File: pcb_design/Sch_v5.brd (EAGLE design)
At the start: 90 x 54 mm, 30 parts

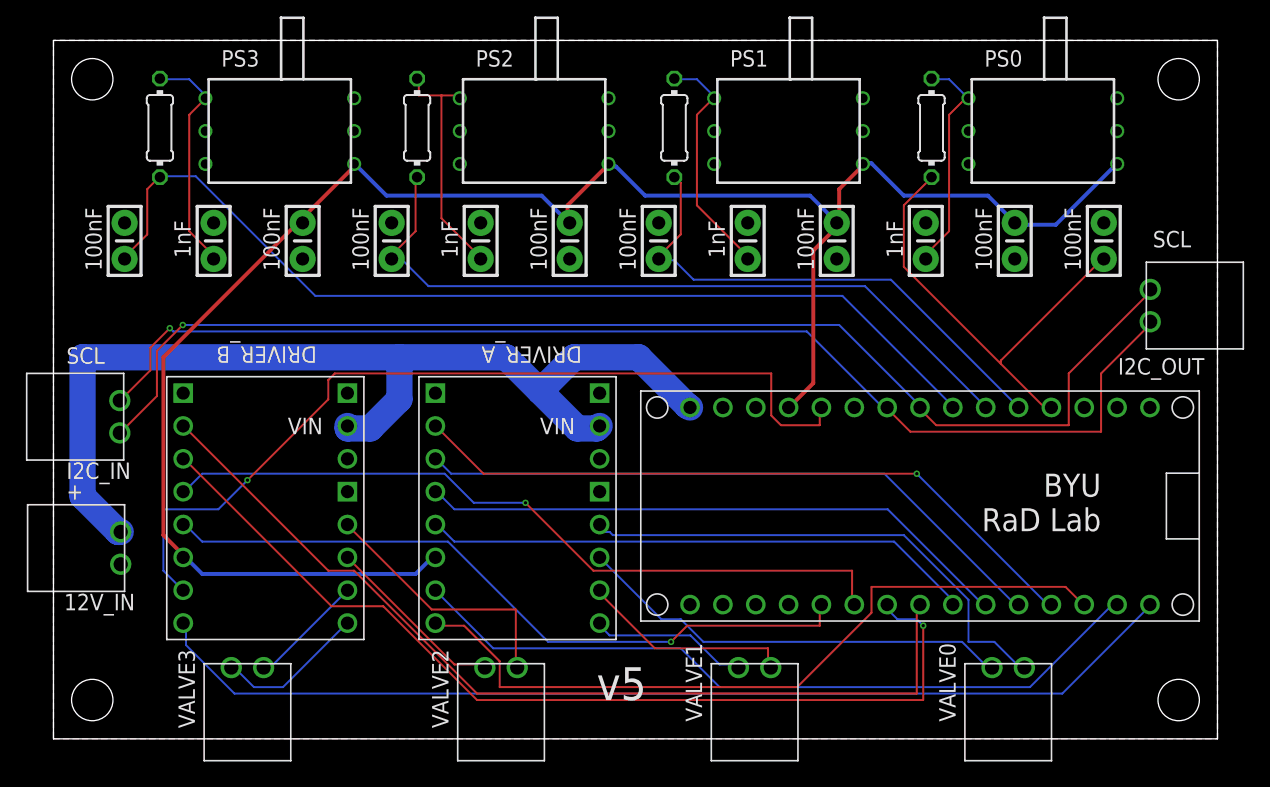
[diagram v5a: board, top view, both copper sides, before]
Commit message: added dip switch. autorouting completed
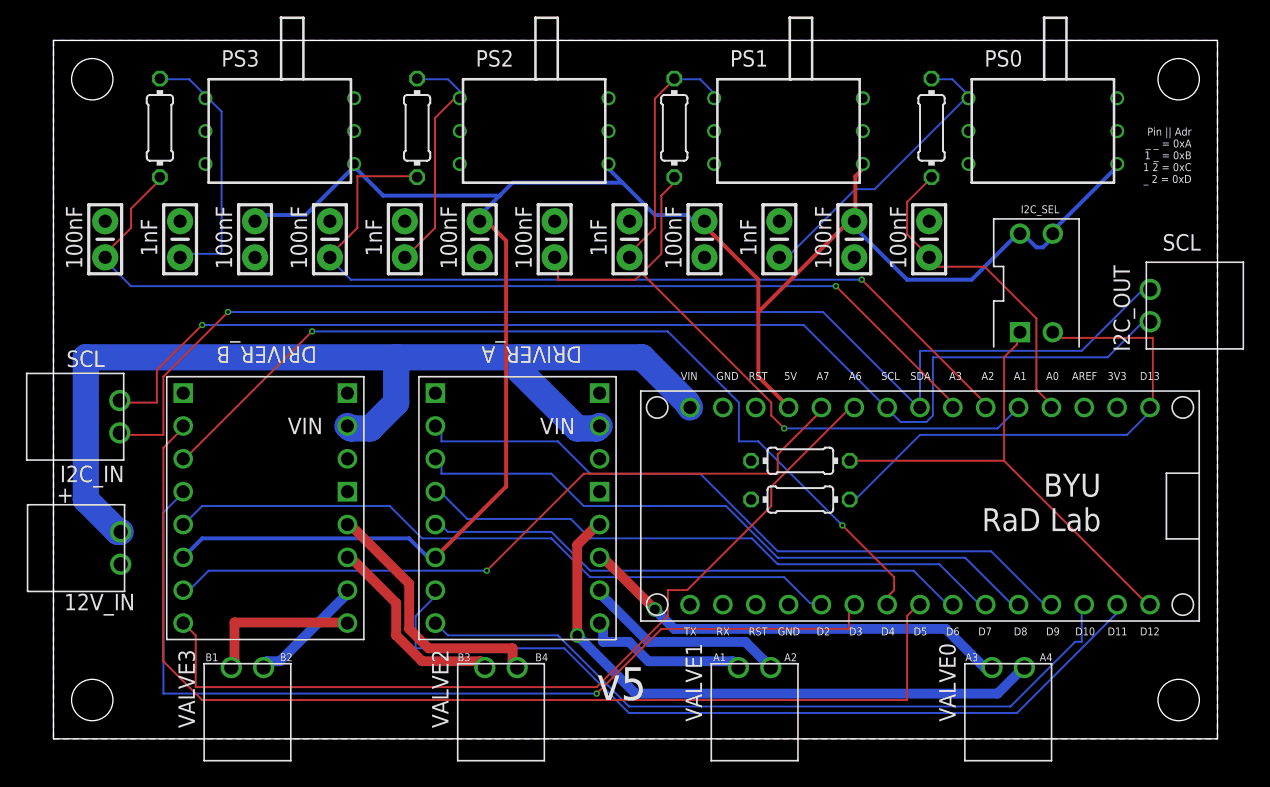
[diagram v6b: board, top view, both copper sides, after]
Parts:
- added I2C_SEL: 2PIN_DIP_DS01-254-S-02BE, byu_pressure_control:2PIN_DIP_DS01-254-S-02BE
- added R5, R6: 4.7k, rcl:0204/7
- moved C9 13.5 mm to (67.7, 38.6)
- moved C7 12.4 mm to (61.9, 38.6)
- moved C1 11.3 mm to (56.1, 38.6)
- moved C8 10.2 mm to (50.3, 38.6)
- moved C2 9.14 mm to (44.5, 38.6)
- moved C10 8.05 mm to (38.8, 38.6)
- moved C6 6.96 mm to (33.0, 38.6)
- moved C3 5.87 mm to (27.2, 38.6)
- moved C11 4.77 mm to (21.4, 38.6)
- moved C5 3.68 mm to (15.6, 38.6)
- moved C4 2.59 mm to (9.79, 38.6)
- moved C12 1.51 mm to (4.00, 38.6)
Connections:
- new net N$13: I2C_SEL.1A, NANO1.30, R6.2
- new net N$14: I2C_SEL.2A, NANO1.1, R5.1
- net 5V: now also I2C_SEL.1B, I2C_SEL.2B
- net EF1_B: now also NANO1.10; no longer NANO1.30
- net GND: now also R5.2, R6.1
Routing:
- net N$14: track 0.00 -> 40.0 mm
- net N$13: track 0.00 -> 38.2 mm
- net D3: track 58.1 -> 73.4 mm
- net EF1_B: track 80.8 -> 67.3 mm
- net D5: track 72.3 -> 85.6 mm
- net A1: track 39.8 -> 52.4 mm, vias 0 -> 1
- net EF2_B: track 67.9 -> 56.3 mm
- net A2: track 57.8 -> 67.5 mm, vias 0 -> 1
- net A0: track 35.2 -> 25.5 mm
- net N$8: track 39.4 -> 46.6 mm, vias 0 -> 1
- net EF2_A: track 58.4 -> 65.5 mm
- net 5V: track 148.1 -> 155.0 mm
- net N$1: track 17.4 -> 23.3 mm
- net D4: track 74.5 -> 71.0 mm, vias 1 -> 2
- net A3: track 76.3 -> 78.6 mm, vias 0 -> 1
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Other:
- board text added: "3V3"
- board text added: "5V"
- board text added: "A0"
- board text added: "A1"
- board text added: "A2"
- board text added: "A3"
- board text added: "A4"
- board text added: "A6"
- board text added: "A7"
- board text added: "AREF"
- board text added: "B1"
- board text added: "B2"
- board text added: "B3"
- board text added: "B4"
- board text added: "D10"
- board text added: "D11"
- board text added: "D12"
- board text added: "D13"
- board text added: "D2"
- board text added: "D3"
- board text added: "D4"
- board text added: "D5"
- board text added: "D6"
- board text added: "D7"
- board text added: "D8"
- board text added: "D9"
- board text added: "GND"
- board text added: "Pin || Adr _ _ = 0xA 1 _ = 0xB 1 2 = 0xC _ 2 = 0xD"
- board text added: "RST"
- board text added: "RX"
- board text added: "SDA"
- board text added: "TX"
- board text added: "VIN"

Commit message: fixed small bug
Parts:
- flipped I2C_OUT to the bottom, turned to 270 degrees
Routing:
- net D4: track 71.0 -> 62.4 mm
- net A3: track 78.6 -> 86.9 mm, vias 1 -> 0
- net A1: track 52.4 -> 59.4 mm, vias 1 -> 0
- net N$13: track 38.2 -> 43.2 mm
- net 5V: track 155.0 -> 157.8 mm
- net SDA: track 95.5 -> 93.0 mm, vias 1 -> 2
- net A0: track 25.5 -> 23.3 mm
- net SCL: track 92.6 -> 93.2 mm
- net D8: track 50.3 -> 49.7 mm

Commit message: fixed another bug
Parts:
- moved I2C_OUT 3.00 mm to (92.0, 36.5), flipped to the top, turned to 90 degrees
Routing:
- net D4: track 62.4 -> 71.0 mm
- net A3: track 86.9 -> 78.6 mm, vias 0 -> 1
- net A1: track 59.4 -> 52.4 mm, vias 0 -> 1
- net SDA: track 93.0 -> 98.5 mm, vias 2 -> 1
- net N$13: track 43.2 -> 38.2 mm
- net 5V: track 157.8 -> 155.0 mm
- net A0: track 23.3 -> 25.5 mm
- net SCL: track 93.2 -> 95.3 mm
- net D8: track 49.7 -> 50.3 mm
